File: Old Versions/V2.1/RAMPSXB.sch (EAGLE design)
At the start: 97 parts, among them CN1 1X4-BIG, CN2 1X4-BIG, CN3 1X4-BIG, CN4 1X4-BIG, CN5 1X4-BIG, CN6 1X4-BIG, CN7 1X4-BIG, CN8 1X4-BIG, CN9 1X4-BIG, J1 1X2-3.5MM, J2 1X2-3.5MM, J3 1X2-3.5MM, J4 1X2-3.5MM, J5 1X2-3.5MM, Q1 PSMN7R0-30YLC, Q2 PSMN7R0-30YLC, Q3 PSMN7R0-30YLC, Q4 PSMN7R0-30YLC

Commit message: Replaced FETs with PSMN7R0-30YLCs for production.
Added Older Version Directory for the old STP55 board. It should also
work as well.
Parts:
- Q1, Q2, Q3, Q4: value PSMN7R0-30YLC -> IRF512; device MyLibrary:PSMN7R0-30YLC -> transistor-power:IRF512
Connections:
- removed net N$45: Q3.4, R17.1
- new net GND1: R10.1
- new net N$49: Q1.G, R15.1
- net GND: now also Q1.S, Q2.S, Q3.S, Q4.S; no longer Q1.1, Q1.2, Q1.3, Q2.1, Q2.2, Q2.3, Q3.1, Q3.2, Q3.3, Q4.1, Q4.2, Q4.3, R10.1
- net N$30: now also Q1.D; no longer Q1.5
- net N$36: now also Q2.D; no longer Q2.5
- net N$37: now also Q3.D; no longer Q3.5
- net N$38: now also Q4.D; no longer Q4.5
- net N$46: now also Q2.G, R16.1; no longer Q4.4, R18.1
- net N$47: now also Q3.G, R17.1; no longer Q2.4, R16.1
- net N$48: now also Q4.G, R18.1; no longer Q1.4, R15.1
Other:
- note added: "stp55nf06l"
- moved on the sheet: R15, R16, R17, R18, R19, R20, R21, R22

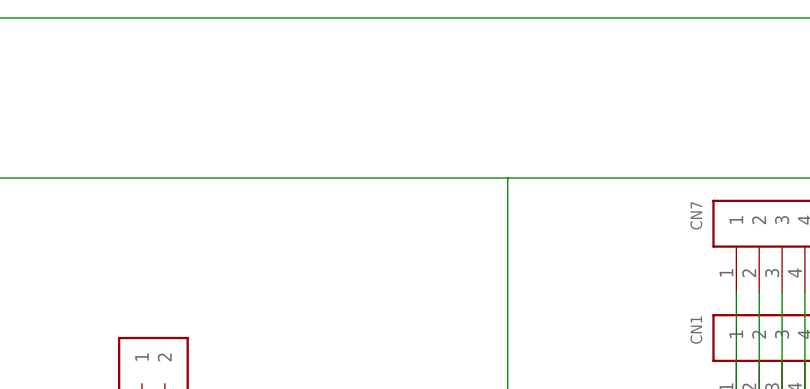
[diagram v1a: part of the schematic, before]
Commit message: Fixed LED Numbering, updated V2.1
LED Indicators were not on the right FETs. Not sure how I missed that.
Updated V2.1 with corrected Vector Text.
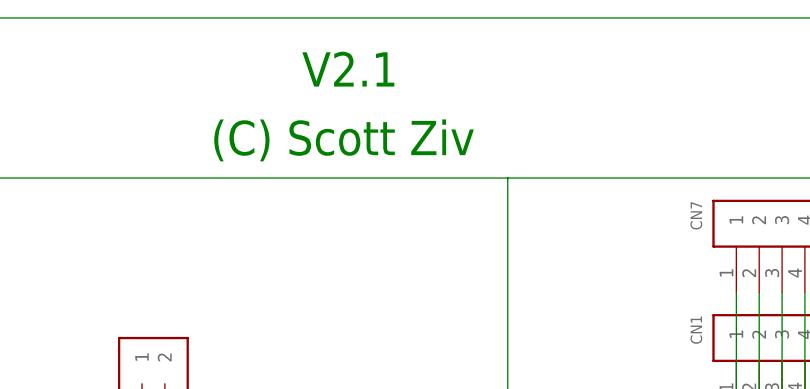
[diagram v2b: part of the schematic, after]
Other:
- note added: "(C) Scott Ziv"
- note added: "V2.1"
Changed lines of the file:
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@@
 <text x="-35.56" y="50.8" size="6.4516" layer="91">RAMPSXB</text>
 <text x="177.8" y="50.8" size="6.4516" layer="91">http://reprap.org/wiki/RAMPSXB</text>
+<text x="81.28" y="53.34" size="3.81" layer="91">V2.1</text>
+<text x="71.12" y="45.72" size="3.81" layer="91">(C) Scott Ziv</text>
 </plain>
 <instances>

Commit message: Fixed some issues with V2.1, and updated gerbers
fixed some stuff with V2.1 and corrected some issues
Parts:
- added LOGO2: OSHW-LOGOL, SparkFun-Aesthetics:OSHW-LOGOL
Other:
- note added: "Developed by SZiv"
- note added: "GPLv3"
- note removed: "(C) Scott Ziv"
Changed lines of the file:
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@@
 <layer number="112" name="tSilk" color="7" fill="1" visible="no" active="yes"/>
 <layer number="113" name="ReferenceLS" color="7" fill="1" visible="no" active="no"/>
+<layer number="114" name="Badge_Outline" color="7" fill="1" visible="no" active="yes"/>
+<layer number="115" name="ReferenceISLANDS" color="7" fill="1" visible="no" active="yes"/>
 <layer number="116" name="Patch_BOT" color="9" fill="4" visible="yes" active="yes"/>
 <layer number="118" name="Rect_Pads" color="7" fill="1" visible="no" active="no"/>
@@
 <part name="R27" library="adafruit" deviceset="R-US_" device="M0805" value="1.8k"/>
 <part name="LED5" library="adafruit" deviceset="LED" device="CHIPLED_0805"/>
+<part name="LOGO2" library="SparkFun-Aesthetics" deviceset="OSHW-LOGO" device="L"/>
 </parts>
 <sheets>
@@
 <text x="177.8" y="50.8" size="6.4516" layer="91">http://reprap.org/wiki/RAMPSXB</text>
 <text x="81.28" y="53.34" size="3.81" layer="91">V2.1</text>
-<text x="71.12" y="45.72" size="3.81" layer="91">(C) Scott Ziv</text>
+<text x="63.5" y="48.26" size="3.81" layer="91">Developed by SZiv</text>
+<text x="134.62" y="50.8" size="3.81" layer="91">GPLv3</text>
 </plain>
 <instances>
@@
 <instance part="R27" gate="G$1" x="60.96" y="5.08" rot="R180"/>
 <instance part="LED5" gate="G$1" x="55.88" y="7.62" rot="R180"/>
+<instance part="LOGO2" gate="G$1" x="33.02" y="53.34"/>
 </instances>
 <busses>
